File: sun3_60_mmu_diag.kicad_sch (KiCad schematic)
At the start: 26 parts, among them J200 SW_Push_SPDT, U200 7188, U201 7188, U202 2168, U203 2168, U205 2168, U206 2168, U207 2168, U208 2168, U210 LS2518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

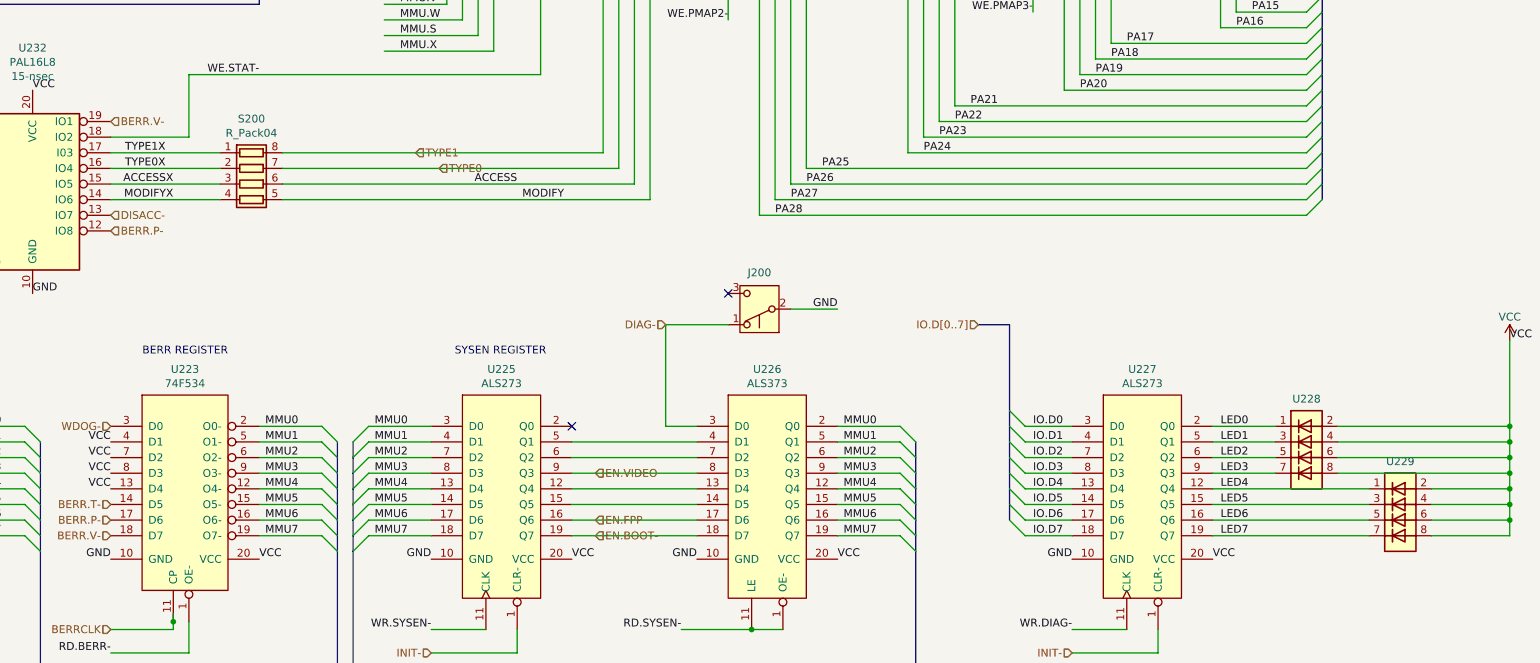
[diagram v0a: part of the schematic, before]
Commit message: Initial layout
- Lay out the PCB to match the original board sans the missing components. No routing yet.
- Pick standard library footprints instead of custom ones for some components.
- Change some ERC errors into warnings - like output pin connected to output pin.
- Change resistor network S200 from DIP to SIP type.
- Set Serial keyboard/mouse section to “Do Not Populate” to gain some space, and it wasn’t going to be used with no video possible anyway. However, in knockout testing with 3.0.1 boot PROM self tests pass, then a warning message tests were interrupted is emitted. Tests then re-run, but system hangs before giving a prompt.
- Fix the LED blocks for the diag register to match the original Dialight 555-4003 part.
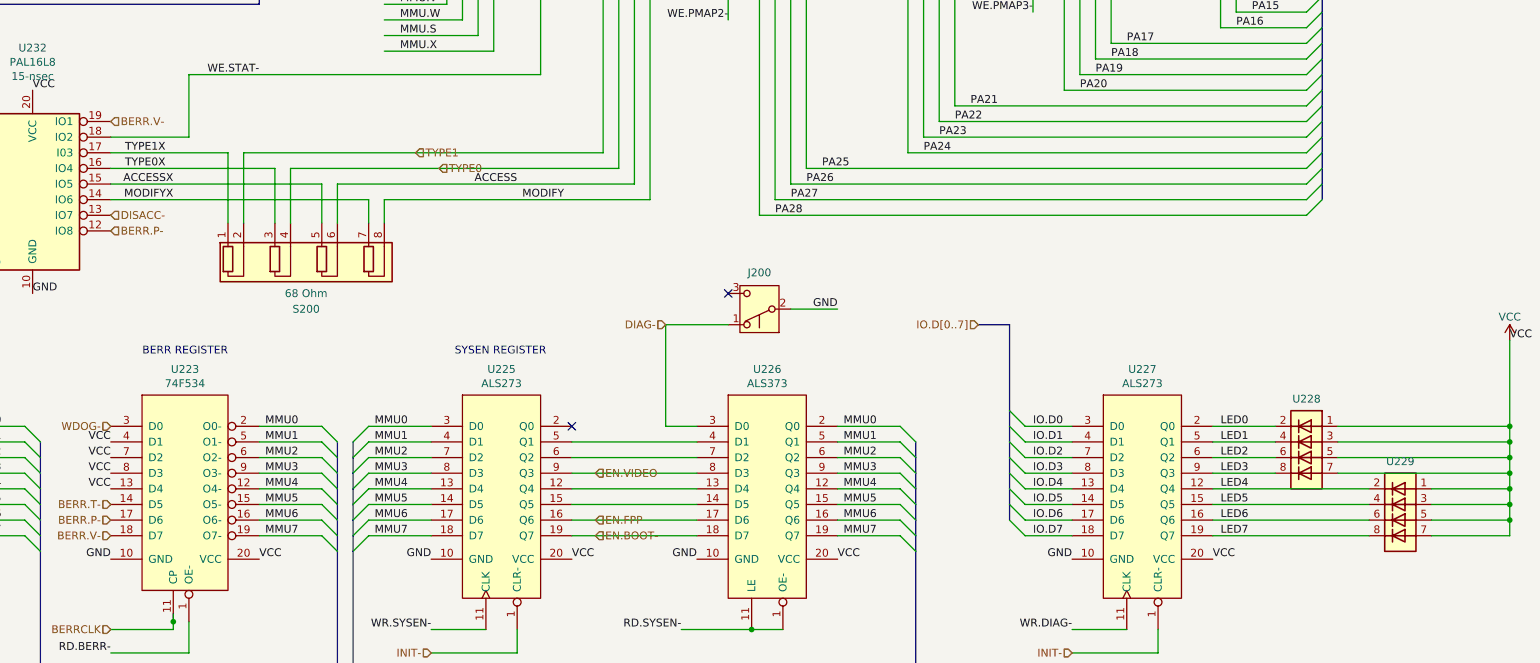
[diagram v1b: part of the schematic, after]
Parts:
- removed S200: R_Pack04, sun3_60:DIP-8_296_ELL, symbol Device:R_Pack04
- added S200: 68 Ohm, Resistor_THT:R_Array_SIP8, symbol Device:R_Pack04_SIP
- J200: value SW_Push_SPDT -> DIAG
- U228, U229: footprint Connector_PinHeader_1.00mm:PinHeader_2x04_P1.00mm_Vertical -> Connector_PinHeader_2.54mm:PinHeader_2x04_P2.54mm_Vertical
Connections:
- net ACCESS: now also S200.6 (R3.2)
- net ACCESSX: now also S200.5 (R3.1)
- net LED0: now also U228.2 (K); no longer U228.1 (A)
- net LED1: now also U228.4; no longer U228.3 (A)
- net LED2: now also U228.6 (K); no longer U228.5
- net LED3: now also U228.8 (K); no longer U228.7
- net LED4: now also U229.2 (K); no longer U229.1 (A)
- net LED5: now also U229.4; no longer U229.3 (A)
- net LED6: now also U229.6 (K); no longer U229.5
- net LED7: now also U229.8 (K); no longer U229.7
- net MODIFY: now also S200.8 (R4.2)
- net MODIFYX: now also S200.7 (R4.1)
- net TYPE0: now also S200.4 (R2.2)
- net TYPE0X: now also S200.3 (R2.1)
- net TYPE1: now also S200.2 (R1.2)
- net TYPE1X: now also S200.1 (R1.1)
- net VCC: now also U228.1 (A), U228.3 (A), U228.5, U228.7, U229.1 (A), U229.3 (A), U229.5, U229.7; no longer U228.2 (K), U228.4, U228.6 (K), U228.8 (K), U229.2 (K), U229.4, U229.6 (K), U229.8 (K)

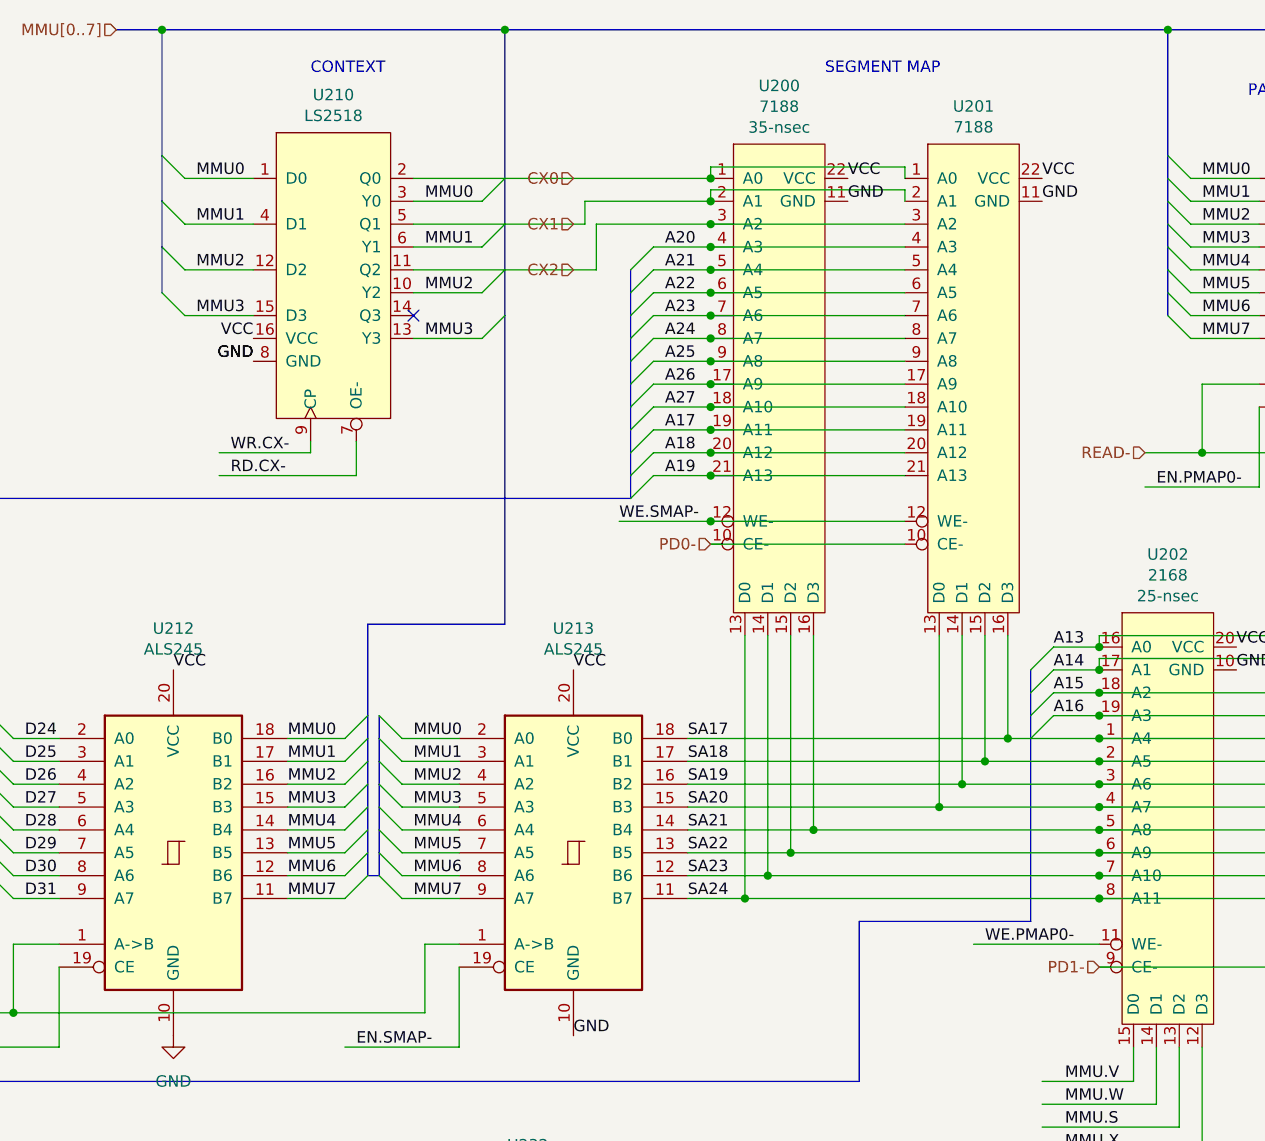
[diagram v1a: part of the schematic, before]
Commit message: Clean up before reorganizing the folders. The schematics and PCB reflect the fixes discovered during the prototype build.
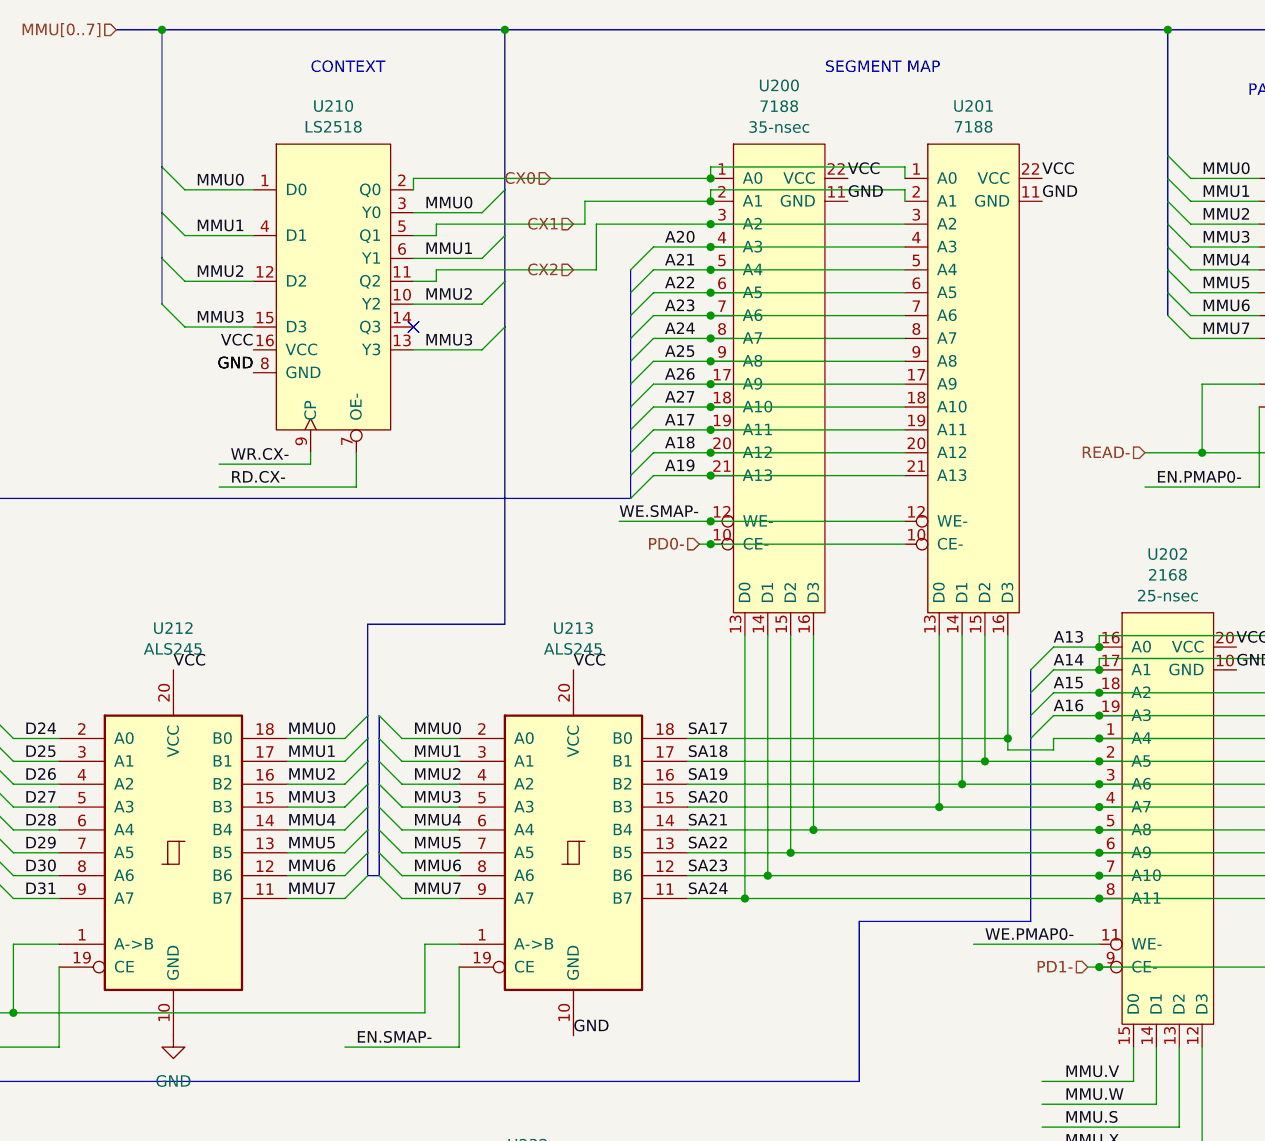
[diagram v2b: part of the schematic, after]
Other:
- moved on the sheet: U210
